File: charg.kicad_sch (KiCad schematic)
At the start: 13 parts, among them IC1 SI3483DDV-T1-BE3, IC2 BQ25302RTER, J1 Screw_Terminal_01x04, J2 Screw_Terminal_01x04, J4 EN

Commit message: No idea
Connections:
- net Earth: now also J1.4 (Pin_4); no longer J1.2 (Pin_2)
- net at C2.1, IC2.2 (REGN): now also J1.2 (Pin_2); no longer J1.3 (Pin_3)
- net at IC2.3 (STAT): now also J1.3 (Pin_3); no longer J1.4 (Pin_4)
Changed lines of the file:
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@@
 (kicad_sch (version 20211123) (generator eeschema)
   (paper "A4")
-  (junction (at 92.71 118.11) (diameter 0) (color 0 0 0 0)
-  )
   (junction (at 102.87 101.6) (diameter 0) (color 0 0 0 0)
   )
@@
   )
   (no_connect (at 134.62 121.92))
+  (bus_entry (at 323.85 40.64) (size 2.54 2.54)
+    (stroke (width 0) (type default) (color 0 0 0 0))
+  )
   (wire (pts (xy 137.16 83.82) (xy 137.16 66.04))
     (stroke (width 0) (type default) (color 0 0 0 0))
@@
     (stroke (width 0) (type default) (color 0 0 0 0))
   )
+  (wire (pts (xy 76.2 113.03) (xy 71.12 113.03))
+    (stroke (width 0) (type default) (color 0 0 0 0))
+  )
   (wire (pts (xy 194.31 96.52) (xy 213.36 96.52))
     (stroke (width 0) (type default) (color 0 0 0 0))
@@
     (stroke (width 0) (type default) (color 0 0 0 0))
   )
-  (wire (pts (xy 78.74 127) (xy 78.74 113.03))
+  (wire (pts (xy 78.74 110.49) (xy 78.74 127))
     (stroke (width 0) (type default) (color 0 0 0 0))
   )
@@
     (stroke (width 0) (type default) (color 0 0 0 0))
   )
+  (wire (pts (xy 78.74 110.49) (xy 71.12 110.49))
+    (stroke (width 0) (type default) (color 0 0 0 0))
+  )
   (wire (pts (xy 180.34 43.18) (xy 180.34 45.72))
     (stroke (width 0) (type default) (color 0 0 0 0))
@@
     (stroke (width 0) (type default) (color 0 0 0 0))
   )
-  (wire (pts (xy 82.55 118.11) (xy 92.71 118.11))
-    (stroke (width 0) (type default) (color 0 0 0 0))
-  )
   (wire (pts (xy 180.34 43.18) (xy 214.63 43.18))
     (stroke (width 0) (type default) (color 0 0 0 0))
@@
     (stroke (width 0) (type default) (color 0 0 0 0))
   )
+  (wire (pts (xy 72.39 123.19) (xy 72.39 115.57))
+    (stroke (width 0) (type default) (color 0 0 0 0))
+  )
   (wire (pts (xy 154.94 100.33) (xy 160.02 100.33))
     (stroke (width 0) (type default) (color 0 0 0 0))
@@
     (stroke (width 0) (type default) (color 0 0 0 0))
   )
-  (wire (pts (xy 82.55 118.11) (xy 82.55 110.49))
-    (stroke (width 0) (type default) (color 0 0 0 0))
-  )
-  (wire (pts (xy 78.74 113.03) (xy 71.12 113.03))
-    (stroke (width 0) (type default) (color 0 0 0 0))
-  )
   (wire (pts (xy 160.02 71.12) (xy 180.34 71.12))
     (stroke (width 0) (type default) (color 0 0 0 0))
   )
-  (wire (pts (xy 82.55 110.49) (xy 71.12 110.49))
-    (stroke (width 0) (type default) (color 0 0 0 0))
-  )
   (wire (pts (xy 102.87 101.6) (xy 102.87 106.68))
     (stroke (width 0) (type default) (color 0 0 0 0))
@@
     (stroke (width 0) (type default) (color 0 0 0 0))
   )
-  (wire (pts (xy 76.2 132.08) (xy 76.2 115.57))
+  (wire (pts (xy 76.2 113.03) (xy 76.2 132.08))
     (stroke (width 0) (type default) (color 0 0 0 0))
   )
@@
     (stroke (width 0) (type default) (color 0 0 0 0))
   )
+  (wire (pts (xy 72.39 115.57) (xy 71.12 115.57))
+    (stroke (width 0) (type default) (color 0 0 0 0))
+  )
   (wire (pts (xy 137.16 121.92) (xy 137.16 138.43))
     (stroke (width 0) (type default) (color 0 0 0 0))
@@
     (stroke (width 0) (type default) (color 0 0 0 0))
   )
-  (wire (pts (xy 92.71 114.3) (xy 92.71 118.11))
-    (stroke (width 0) (type default) (color 0 0 0 0))
-  )
   (wire (pts (xy 78.74 99.06) (xy 92.71 99.06))
     (stroke (width 0) (type default) (color 0 0 0 0))
@@
     (stroke (width 0) (type default) (color 0 0 0 0))
   )
-  (wire (pts (xy 92.71 118.11) (xy 92.71 119.38))
+  (wire (pts (xy 92.71 114.3) (xy 92.71 119.38))
     (stroke (width 0) (type default) (color 0 0 0 0))
   )
@@
   )
   (wire (pts (xy 124.46 71.12) (xy 124.46 99.06))
-    (stroke (width 0) (type default) (color 0 0 0 0))
-  )
-  (wire (pts (xy 76.2 115.57) (xy 71.12 115.57))
     (stroke (width 0) (type default) (color 0 0 0 0))
   )
@@
     )
     (property "Vin" "Vin" (id 4) (at 60.96 107.95 0))
-    (property "GND" "GND" (id 5) (at 60.96 110.49 0))
-    (property "Field6" "REGN" (id 6) (at 60.96 113.03 0))
-    (property "Field7" "STAT" (id 7) (at 60.96 115.57 0))
+    (property "GND" "GND" (id 5) (at 60.96 115.57 0))
+    (property "Field6" "REGN" (id 6) (at 60.96 110.49 0))
+    (property "Field7" "STAT" (id 7) (at 60.96 113.03 0))
     (pin "1")
     (pin "2")
@@
     (pin "2")
   )
+  (symbol (lib_id "power:Earth") (at 72.39 123.19 0) (unit 1)
+    (in_bom yes) (on_board yes) (fields_autoplaced)
+    (property "Reference" "#PWR?" (id 0) (at 72.39 129.54 0)
+      (effects (font (size 1.27 1.27)) hide)
+    )
+    (property "Value" "Earth" (id 1) (at 72.39 127 0)
+      (effects (font (size 1.27 1.27)) hide)
+    )
+    (property "Footprint" "" (id 2) (at 72.39 123.19 0)
+      (effects (font (size 1.27 1.27)) hide)
+    )
+    (property "Datasheet" "~" (id 3) (at 72.39 123.19 0)
+      (effects (font (size 1.27 1.27)) hide)
+    )
+    (pin "1")
+  )
   (symbol (lib_id "power:Earth") (at 102.87 119.38 0) (unit 1)
     (in_bom yes) (on_board yes) (fields_autoplaced)
@@
       (reference "#PWR010") (unit 1) (value "Earth") (footprint "")
     )
+    (path "/a0e0f6a5-c4eb-4570-a224-24e9ef1a5d88"
+      (reference "#PWR?") (unit 1) (value "Earth") (footprint "")
+    )
     (path "/b9a740b3-1199-4755-a81b-90abafe42fd7"

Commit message: FInal...I guess
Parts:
- D2: footprint Schottky dd:DIOM5026X220N -> Schottky DD with stock:DIOM5126X265N
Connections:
- net Earth: now also J2.1 (Pin_1); no longer J2.4 (Pin_4)
- net at C5.1, IC1.1 (D_1), IC1.2 (D_2)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: now also J2.3 (Pin_3); no longer J2.2 (Pin_2)
- net at C3.1, IC1.4 (S), IC2.16 (PMID): now also J2.4 (Pin_4); no longer J2.1 (Pin_1)
- net at IC2.7 (TS): now also J2.2 (Pin_2); no longer J2.3 (Pin_3)
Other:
- moved on the sheet: J2
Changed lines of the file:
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@@
+    (stroke (width 0) (type default) (color 0 0 0 0))
+  )
+  (wire (pts (xy 212.09 83.82) (xy 212.09 80.01))
     (stroke (width 0) (type default) (color 0 0 0 0))
   )
@@
     (stroke (width 0) (type default) (color 0 0 0 0))
   )
+  (wire (pts (xy 224.79 85.09) (xy 246.38 85.09))
+    (stroke (width 0) (type default) (color 0 0 0 0))
+  )
   (wire (pts (xy 99.06 101.6) (xy 99.06 127))
     (stroke (width 0) (type default) (color 0 0 0 0))
@@
     (stroke (width 0) (type default) (color 0 0 0 0))
   )
+  (wire (pts (xy 214.63 83.82) (xy 212.09 83.82))
+    (stroke (width 0) (type default) (color 0 0 0 0))
+  )
   (wire (pts (xy 185.42 71.12) (xy 185.42 74.93))
     (stroke (width 0) (type default) (color 0 0 0 0))
@@
     (stroke (width 0) (type default) (color 0 0 0 0))
   )
+  (wire (pts (xy 213.36 86.36) (xy 210.82 86.36))
+    (stroke (width 0) (type default) (color 0 0 0 0))
+  )
   (wire (pts (xy 181.61 87.63) (xy 181.61 88.9))
     (stroke (width 0) (type default) (color 0 0 0 0))
@@
     (stroke (width 0) (type default) (color 0 0 0 0))
   )
+  (wire (pts (xy 224.79 88.9) (xy 224.79 85.09))
+    (stroke (width 0) (type default) (color 0 0 0 0))
+  )
   (wire (pts (xy 160.02 71.12) (xy 180.34 71.12))
     (stroke (width 0) (type default) (color 0 0 0 0))
@@
     (stroke (width 0) (type default) (color 0 0 0 0))
   )
+  (wire (pts (xy 212.09 80.01) (xy 246.38 80.01))
+    (stroke (width 0) (type default) (color 0 0 0 0))
+  )
   (wire (pts (xy 166.37 96.52) (xy 194.31 96.52))
     (stroke (width 0) (type default) (color 0 0 0 0))
   )
-  (wire (pts (xy 222.25 91.44) (xy 224.79 91.44))
+  (wire (pts (xy 210.82 82.55) (xy 246.38 82.55))
+    (stroke (width 0) (type default) (color 0 0 0 0))
+  )
+  (wire (pts (xy 246.38 87.63) (xy 226.06 87.63))
+    (stroke (width 0) (type default) (color 0 0 0 0))
+  )
+  (wire (pts (xy 222.25 91.44) (xy 226.06 91.44))
     (stroke (width 0) (type default) (color 0 0 0 0))
   )
@@
     (stroke (width 0) (type default) (color 0 0 0 0))
   )
-  (wire (pts (xy 224.79 86.36) (xy 213.36 86.36))
-    (stroke (width 0) (type default) (color 0 0 0 0))
-  )
   (wire (pts (xy 76.2 113.03) (xy 76.2 132.08))
     (stroke (width 0) (type default) (color 0 0 0 0))
@@
     (stroke (width 0) (type default) (color 0 0 0 0))
   )
+  (wire (pts (xy 210.82 86.36) (xy 210.82 82.55))
+    (stroke (width 0) (type default) (color 0 0 0 0))
+  )
   (wire (pts (xy 99.06 101.6) (xy 102.87 101.6))
     (stroke (width 0) (type default) (color 0 0 0 0))
@@
     (stroke (width 0) (type default) (color 0 0 0 0))
   )
-  (wire (pts (xy 224.79 83.82) (xy 214.63 83.82))
-    (stroke (width 0) (type default) (color 0 0 0 0))
-  )
   (wire (pts (xy 194.31 96.52) (xy 194.31 80.01))
     (stroke (width 0) (type default) (color 0 0 0 0))
@@
   )
   (wire (pts (xy 152.4 76.2) (xy 152.4 80.01))
+    (stroke (width 0) (type default) (color 0 0 0 0))
+  )
+  (wire (pts (xy 226.06 91.44) (xy 226.06 87.63))
     (stroke (width 0) (type default) (color 0 0 0 0))
   )
@@
     (pin "2")
   )
-  (symbol (lib_id "Connector:Screw_Terminal_01x04") (at 229.87 86.36 0) (unit 1)
+  (symbol (lib_id "Connector:Screw_Terminal_01x04") (at 251.46 85.09 0) (mirror x) (unit 1)
     (in_bom yes) (on_board yes)
-    (property "Reference" "J2" (id 0) (at 229.87 77.47 0))
-    (property "Value" "Screw_Terminal_01x04" (id 1) (at 229.87 80.01 0))
-    (property "Footprint" "Boost LTC3426:TerminalBlock_MetzConnect_Type059_RT06304HBWC_1x04_P3.50mm_Horizontal" (id 2) (at 229.87 86.36 0)
-      (effects (font (size 1.27 1.27)) hide)
-    )
-    (property "Datasheet" "~" (id 3) (at 229.87 86.36 0)
-      (effects (font (size 1.27 1.27)) hide)
-    )
-    (property "Vin" "Vout" (id 4) (at 234.95 83.82 0))
-    (property "GND" "Vbatt" (id 5) (at 234.95 86.36 0))
-    (property "Field6" "Thermy" (id 6) (at 234.95 88.9 0))
-    (property "Field7" "GND" (id 7) (at 234.95 91.44 0))
+    (property "Reference" "J2" (id 0) (at 251.46 93.98 0))
+    (property "Value" "Screw_Terminal_01x04" (id 1) (at 251.46 91.44 0))
+    (property "Footprint" "Boost LTC3426:TerminalBlock_MetzConnect_Type059_RT06304HBWC_1x04_P3.50mm_Horizontal" (id 2) (at 251.46 85.09 0)
+      (effects (font (size 1.27 1.27)) hide)
+    )
+    (property "Datasheet" "~" (id 3) (at 251.46 85.09 0)
+      (effects (font (size 1.27 1.27)) hide)
+    )
+    (property "Vin" "Vout" (id 4) (at 256.54 80.01 0))
+    (property "GND" "Vbatt" (id 5) (at 256.54 82.55 0))
+    (property "Field6" "Thermy" (id 6) (at 256.54 85.09 0))
+    (property "Field7" "GND" (id 7) (at 256.54 87.63 0))
     (pin "1")
     (pin "2")
@@
     (property "Reference" "D2" (id 0) (at 156.21 68.58 0))
     (property "Value" "RBR3L40ADD" (id 1) (at 157.48 73.66 0))
-    (property "Footprint" "Schottky dd:DIOM5026X220N" (id 2) (at 156.21 71.12 0)
+    (property "Footprint" "Schottky DD with stock:DIOM5126X265N" (id 2) (at 156.21 71.12 0)
       (effects (font (size 1.27 1.27)) hide)
     )
@@
   (symbol (lib_id "power:Earth") (at 72.39 123.19 0) (unit 1)
     (in_bom yes) (on_board yes) (fields_autoplaced)
-    (property "Reference" "#PWR?" (id 0) (at 72.39 129.54 0)
+    (property "Reference" "#PWR0101" (id 0) (at 72.39 129.54 0)
       (effects (font (size 1.27 1.27)) hide)
     )
@@
     )
     (path "/a0e0f6a5-c4eb-4570-a224-24e9ef1a5d88"
-      (reference "#PWR?") (unit 1) (value "Earth") (footprint "")
+      (reference "#PWR0101") (unit 1) (value "Earth") (footprint "")
     )
     (path "/b9a740b3-1199-4755-a81b-90abafe42fd7"
@@
     )
     (path "/64e04f30-b75a-485a-9e25-e618219d18d5"
-      (reference "D2") (unit 1) (value "RBR3L40ADD") (footprint "Schottky dd:DIOM5026X220N")
+      (reference "D2") (unit 1) (value "RBR3L40ADD") (footprint "Schottky DD with stock:DIOM5126X265N")
     )
     (path "/ff90fce7-88c8-4858-850a-5a7e1e5af2e0"

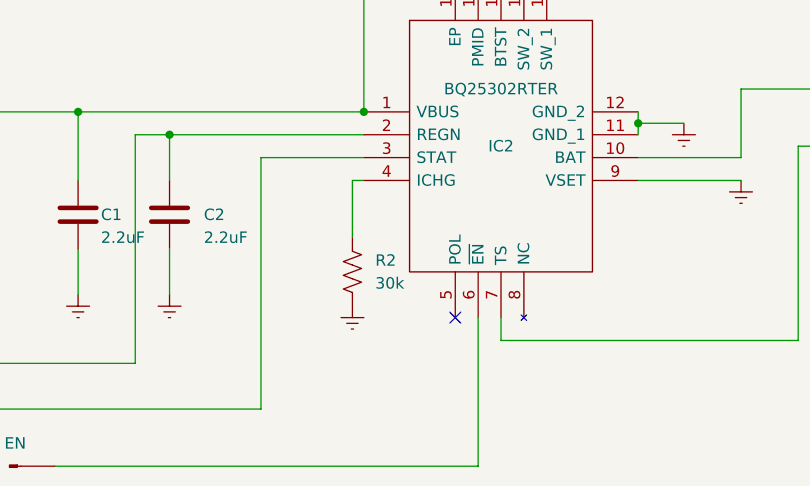
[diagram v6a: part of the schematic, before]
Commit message: Replace 30k ISEt with 30.9k
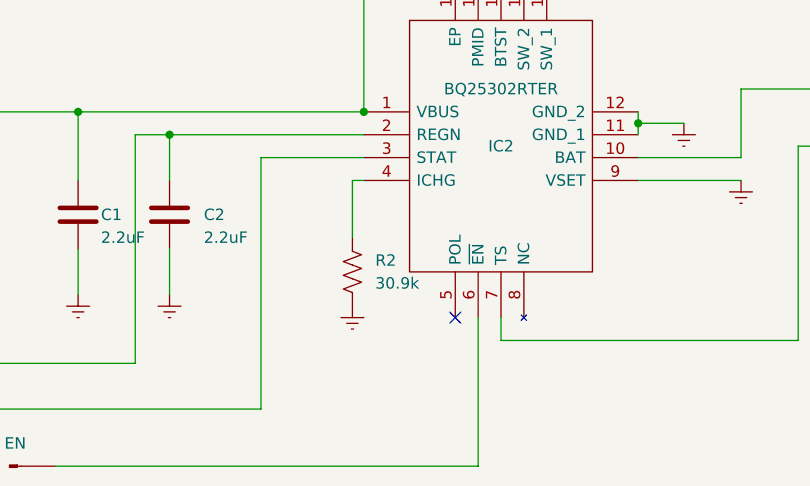
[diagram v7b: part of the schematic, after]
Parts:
- R2: value 30k -> 30.9k; footprint 30k rst:RESC2012X70N -> rst 30.9k:RC0603FR-0730K9L
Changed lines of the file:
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@@
       (effects (font (size 1.27 1.27)) (justify right))
     )
-    (property "Value" "30k" (id 1) (at 125.73 118.1099 0)
+    (property "Value" "30.9k" (id 1) (at 125.73 118.1099 0)
       (effects (font (size 1.27 1.27)) (justify right))
     )
-    (property "Footprint" "30k rst:RESC2012X70N" (id 2) (at 122.174 116.586 90)
+    (property "Footprint" "rst 30.9k:RC0603FR-0730K9L" (id 2) (at 122.174 116.586 90)
       (effects (font (size 1.27 1.27)) hide)
     )
@@
     )
     (path "/0c790e80-edef-4eb3-9ffb-25a86ba2e232"
-      (reference "R2") (unit 1) (value "30k") (footprint "30k rst:RESC2012X70N")
-    )
-  )
+      (reference "R2") (unit 1) (value "30.9k") (footprint "rst 30.9k:RC0603FR-0730K9L")
+    )
+  )
